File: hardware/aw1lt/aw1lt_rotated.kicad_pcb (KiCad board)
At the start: 2 copper layers, 30 x 22 mm, 27 parts, among them J1 ISP_FTDI, Q1 Q_NPN_CBE, SW1 SW_Push, SW2 SW_Push, SW3 SW_Push, U1 DS3231MZ, U2 ATMEGA328P-AU

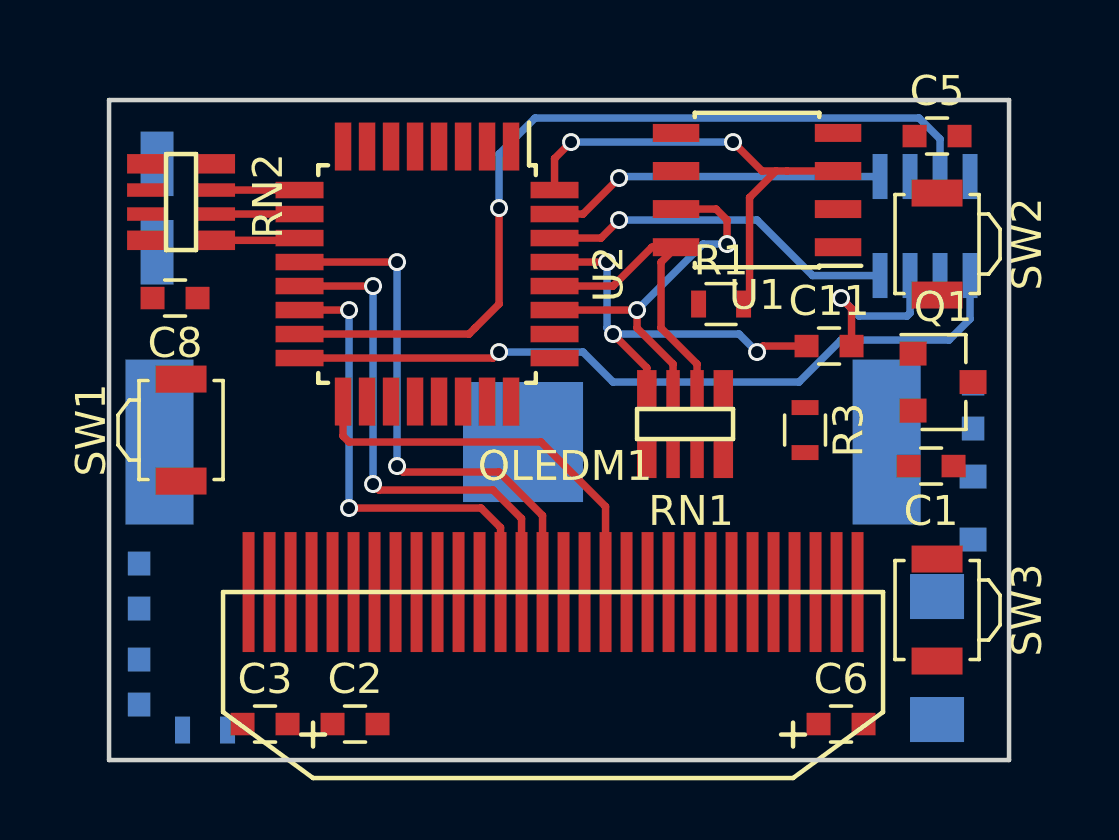
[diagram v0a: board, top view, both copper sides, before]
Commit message: more routing, have a separate board for a rotated uc
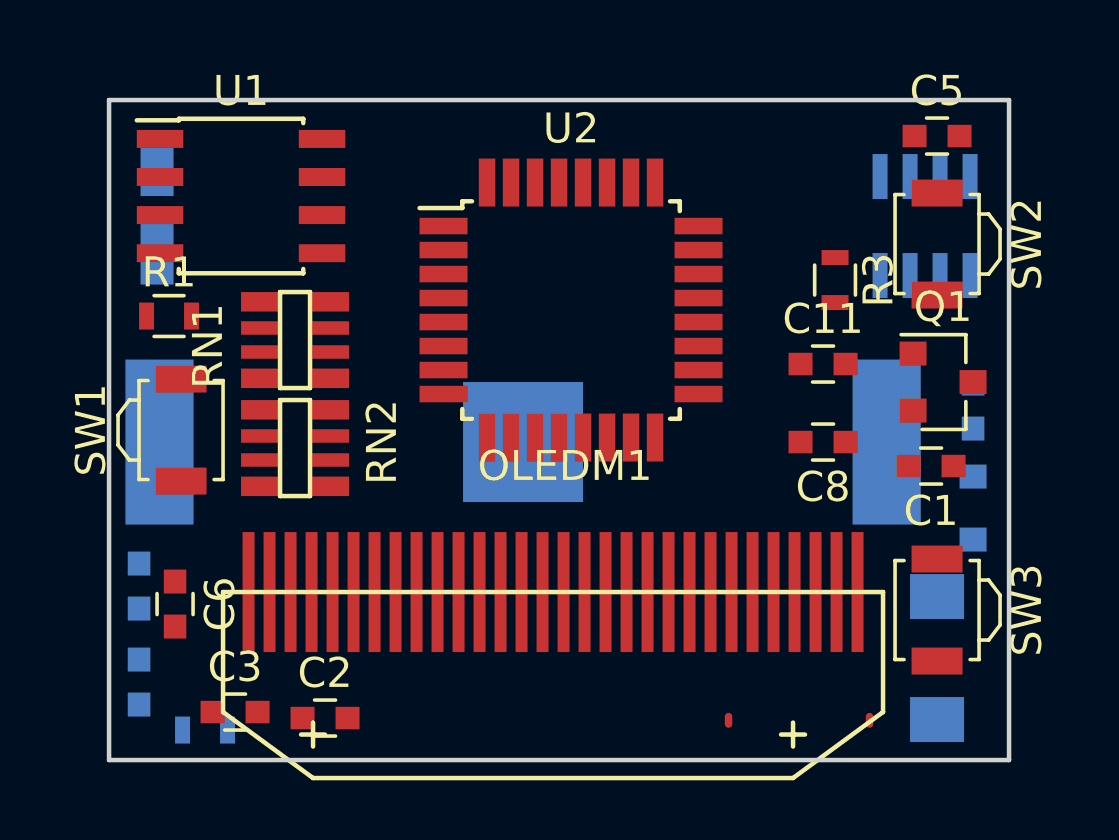
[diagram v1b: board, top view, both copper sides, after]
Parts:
- moved C6 22.6 mm to (127.2, 141.8), turned to 270 degrees
- moved C8 22.1 mm to (148.8, 136.4)
- moved R1 18.4 mm to (127.0, 132.2)
- moved U1 17.2 mm to (129.4, 128.2), turned to 0 degrees
- moved RN1 13.3 mm to (131.2, 133.0), turned to 270 degrees
- moved RN2 9.04 mm to (131.2, 136.6)
- moved R3 5.10 mm to (149.2, 131.0)
- moved U2 4.95 mm to (140.4, 132.0), turned to 0 degrees
- moved C3 1.08 mm to (129.2, 145.4)
- moved C2 1.02 mm to (132.2, 145.6)
- moved C11 0.63 mm to (148.8, 133.8)
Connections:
- U2 pad 23: A1 -> SPKR
- U2 pad 24: SPKR -> A1
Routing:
- net MOSI: track 28.8 -> 0.00 mm, vias 1 -> 0
- net MISO: track 25.2 -> 0.00 mm, vias 1 -> 0
- net D8: track 18.1 -> 0.00 mm, vias 2 -> 0
- net D9: track 16.9 -> 0.00 mm, vias 2 -> 0
- net INT0: track 16.0 -> 0.00 mm, vias 2 -> 0
- net CS: track 15.7 -> 0.00 mm, vias 2 -> 0
- net SCK: track 13.7 -> 0.00 mm
- net Net-(C11-Pad1): track 13.1 -> 0.00 mm, vias 3 -> 0
- net SDA: track 12.5 -> 0.00 mm, vias 2 -> 0
- net RXD: track 11.9 -> 0.00 mm, vias 1 -> 0
- net TXD: track 11.4 -> 0.00 mm, vias 1 -> 0
- net SCL: track 10.0 -> 0.00 mm
- net DTR: track 5.58 -> 0.00 mm, vias 1 -> 0
- net PB2: track 2.94 -> 0.00 mm
- net PB1: track 2.80 -> 0.00 mm
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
